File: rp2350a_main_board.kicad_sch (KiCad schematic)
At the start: 65 parts, among them J1 USB_C_Receptacle_USB2.0_16P, J2 Micro_SD_Card_Det1, J3 Conn_02x10_Odd_Even, J4 SM03B-SRSS-TB, J5 SM03B-SRSS-TB, J6 Conn_02x10_Odd_Even, SW1 SW_Push, SW2 SW_Push, U1 RP2350_60QFN, U2 W25Q16JVSS, U3 APS1604M-3SQRx-SN, U4 AP2112K-3.3, Y1 ABM8-272-T3

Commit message: V1.0.0
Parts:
- removed C12: 100n, Capacitor_SMD:C_0402_1005Metric_Pad0.74x0.62mm_HandSolder, symbol Device:C
- removed C24: 10u, Capacitor_SMD:C_0603_1608Metric_Pad1.08x0.95mm_HandSolder, symbol Device:C
- removed J3, J6: Conn_02x10_Odd_Even, Connector_PinSocket_2.54mm:PinSocket_2x10_P2.54mm_Vertical, symbol Connector_Generic:Conn_02x10_Odd_Even
- removed RN1, RN2: 10k, Resistor_SMD:R_Array_Convex_4x0603, symbol Device:R_Pack04_Split
- removed U4: AP2112K-3.3, Package_TO_SOT_SMD:SOT-23-5, symbol Regulator_Linear:AP2112K-3.3
- added J3, J6: Conn_02x12, Connector_PinSocket_2.54mm:PinSocket_2x12_P2.54mm_Vertical, symbol Connector_Generic:Conn_02x12_Odd_Even
- added J7, J8: Conn_02x12, Connector_PinSocket_2.54mm:PinSocket_2x12_P2.54mm_Vertical_SMD, symbol Connector_Generic:Conn_02x12_Odd_Even
- added L2: 470n, Library:Inductor_SMD_L_4.0x4.0_H1.5, symbol Device:L
- added R20: 511k, Resistor_SMD:R_0402_1005Metric_Pad0.72x0.64mm_HandSolder, symbol Device:R
- added R21: 91k, Resistor_SMD:R_0402_1005Metric_Pad0.72x0.64mm_HandSolder, symbol Device:R
- added R22, R23, R24: 10k, Resistor_SMD:R_0402_1005Metric_Pad0.72x0.64mm_HandSolder, symbol Device:R
- added R25: 33k, Resistor_SMD:R_0402_1005Metric_Pad0.72x0.64mm_HandSolder, symbol Device:R
- added SW3: SW_SPDT, Button_Switch_SMD:SW_SPDT_CK_JS102011SAQN, symbol Switch:SW_SPDT
- added TP1: ST, TestPoint:TestPoint_Pad_D1.0mm, symbol Connector:TestPoint
- added TP2: EN, TestPoint:TestPoint_Pad_D1.0mm, symbol Connector:TestPoint
- added TP4: PG, TestPoint:TestPoint_Pad_D1.0mm, symbol Connector:TestPoint
- added U4: TPS63802, Library:TPS63802, symbol New_Library:TPS63802
- added U5: TPS2116DRL, Package_TO_SOT_SMD:SOT-583-8, symbol Power_Management:TPS2116DRL
- C3, C4: footprint Capacitor_SMD:C_0603_1608Metric_Pad1.08x0.95mm_HandSolder -> Capacitor_SMD:C_0402_1005Metric_Pad0.74x0.62mm_HandSolder
- D1, D2: footprint LED_SMD:LED_0805_2012Metric -> LED_SMD:LED_0805_2012Metric_Pad1.15x1.40mm_HandSolder
- R1, R2, R6: footprint Resistor_SMD:R_0805_2012Metric_Pad1.20x1.40mm_HandSolder -> Resistor_SMD:R_0402_1005Metric_Pad0.72x0.64mm_HandSolder
- R11: value 470 -> 1k; footprint Resistor_SMD:R_0603_1608Metric_Pad0.98x0.95mm_HandSolder -> Resistor_SMD:R_0402_1005Metric_Pad0.72x0.64mm_HandSolder
- R7, R8, R9: footprint Resistor_SMD:R_0805_2012Metric_Pad1.20x1.40mm_HandSolder -> Resistor_SMD:R_0402_1005Metric_Pad0.72x0.64mm_HandSolder; now in the parts list
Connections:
- net +3V3: now also C22.1, J3.1 (Pin_1), J3.2 (Pin_2), J3.3 (Pin_3), J3.4 (Pin_4), J6.7 (Pin_7), J6.8 (Pin_8), J7.1 (Pin_1), J7.2 (Pin_2), J7.3 (Pin_3), J7.4 (Pin_4), J8.7 (Pin_7), J8.8 (Pin_8), R20.1, U4.6 (VOUT)
- net GND: now also J3.11 (Pin_11), J3.12 (Pin_12), J3.17 (Pin_17), J3.18 (Pin_18), J3.23 (Pin_23), J3.24 (Pin_24), J3.5 (Pin_5), J3.6 (Pin_6), J6.13 (Pin_13), J6.14 (Pin_14), J6.19 (Pin_19), J6.20 (Pin_20), J6.23 (Pin_23), J6.24 (Pin_24), J7.11 (Pin_11), J7.12 (Pin_12), J7.17 (Pin_17), J7.18 (Pin_18), J7.23 (Pin_23), J7.24 (Pin_24), J7.5 (Pin_5), J7.6 (Pin_6), J8.13 (Pin_13), J8.14 (Pin_14), J8.19 (Pin_19), J8.20 (Pin_20), J8.23 (Pin_23), J8.24 (Pin_24), R21.2, R24.2, U4.2 (MODE), U4.3 (AGND), U4.8 (GND), U5.1 (GND); no longer U1.15 (GPIO11), U1.17 (GPIO13), U1.19 (GPIO15), U1.28 (GPIO17), U1.31 (GPIO19)
- net GPIO10: now also J3.10 (Pin_10), J7.10 (Pin_10)
- net GPIO12: now also J3.14 (Pin_14), J7.14 (Pin_14)
- net GPIO14: now also J3.16 (Pin_16), J7.16 (Pin_16)
- net GPIO16: now also J3.20 (Pin_20), J7.20 (Pin_20)
- net GPIO18: now also J3.22 (Pin_22), J7.22 (Pin_22)
- net GPIO20: now also J6.21 (Pin_21), J8.21 (Pin_21)
- net GPIO21: now also J6.22 (Pin_22), J8.22 (Pin_22)
- net GPIO22: now also J6.17 (Pin_17), J8.17 (Pin_17)
- net GPIO23: now also J6.18 (Pin_18), J8.18 (Pin_18)
- net GPIO24: now also J6.15 (Pin_15), J8.15 (Pin_15)
- net GPIO25: now also J6.16 (Pin_16), J8.16 (Pin_16)
- net GPIO26_ADC0: now also J6.11 (Pin_11), J8.11 (Pin_11)
- net GPIO27_ADC1: now also J6.12 (Pin_12), J8.12 (Pin_12)
- net GPIO28_ADC2: now also J6.9 (Pin_9), J8.9 (Pin_9)
- net GPIO29_ADC3: now also J6.10 (Pin_10), J8.10 (Pin_10)
- net GPIO9: now also J3.7 (Pin_7), J7.7 (Pin_7)
- net RUN: now also J3.8 (Pin_8), J7.8 (Pin_8)
- net VBUS renamed VUSB
- net VUSB: now also J6.1 (Pin_1), J6.2 (Pin_2), J8.1 (Pin_1), J8.2 (Pin_2), R25.1, U5.3 (VIN1), U5.5 (MODE); no longer C21.1, C22.1
- new net: R20.2, R21.1, U4.4 (FB)
- new net: R22.2, TP2.1, U4.1 (EN)
- new net: TP4.1, U4.5 (PG)
- new net: R23.1, SW3.1 (A), U5.2 (VOUT), U5.7 (VOUT)
- new net: R24.1, R25.2, U5.4 (PR1)
- new net: R23.2, TP1.1, U5.8 (ST)
- new net GPIO11: J3.9 (Pin_9), J7.9 (Pin_9), U1.15 (GPIO11)
- new net GPIO13: J3.13 (Pin_13), J7.13 (Pin_13), U1.17 (GPIO13)
- new net GPIO15: J3.15 (Pin_15), J7.15 (Pin_15), U1.19 (GPIO15)
- new net GPIO17: J3.19 (Pin_19), J7.19 (Pin_19), U1.28 (GPIO17)
- new net GPIO19: J3.21 (Pin_21), J7.21 (Pin_21), U1.31 (GPIO19)
- new net PS_L1: L2.1, U4.9 (L1)
- new net PS_L2: L2.2, U4.7 (L2)
- new net VBAT: J6.3 (Pin_3), J6.4 (Pin_4), J8.3 (Pin_3), J8.4 (Pin_4), U5.6 (VIN2)
- new net VIN: C21.1, J6.5 (Pin_5), J6.6 (Pin_6), J8.5 (Pin_5), J8.6 (Pin_6), R22.1, SW3.2 (B), U4.10 (VIN)
- no-connect marks 4 -> 3
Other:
- note added: "Power"
- note added: "Power Selection"
- note removed: "Power (placeholder)"
- moved on the sheet: R13, R14, R15, R16, R17, R18, R19

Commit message: Clean up component references
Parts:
- renumbered C21 to C1, C14 to C10, C15 to C11, C16 to C12, C17 to C13, C18 to C14, C19 to C15, C1 to C16, C8 to C17, C7 to C18, C6 to C19, C22 to C2, C2 to C20, C4 to C21, C3 to C22, C23 to C3, C5 to C4, C20 to C5, C9 to C6, C10 to C7, C11 to C8, C13 to C9, J5 to J2, J2 to J3, J3 to J5, L2 to L1, L1 to L2, R22 to R1, R2 to R10, R16 to R11, R19 to R12, R11 to R13, R25 to R14, R12 to R15, R23 to R16, R24 to R17, R5 to R18, R3 to R19, R17 to R2, R4 to R20, R10 to R21, R6 to R22, R9 to R23, R7 to R24, R8 to R25, R20 to R3, R18 to R4, R14 to R5, R21 to R6, R13 to R7, R15 to R8, R1 to R9, SW3 to SW1, SW1 to SW2, SW2 to SW3, TP2 to TP1, TP4 to TP2, TP1 to TP3, U4 to U1, U5 to U2, U2 to U3, U1 to U4, U3 to U5

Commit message: Update BOM list
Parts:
- R12, R21, R22: now in the parts list
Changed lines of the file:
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@@
 		(unit 1)
 		(exclude_from_sim no)
-		(in_bom no)
+		(in_bom yes)
 		(on_board yes)
 		(dnp no)
@@
 		(unit 1)
 		(exclude_from_sim no)
-		(in_bom no)
+		(in_bom yes)
 		(on_board yes)
 		(dnp no)
@@
 		(unit 1)
 		(exclude_from_sim no)
-		(in_bom no)
+		(in_bom yes)
 		(on_board yes)
 		(dnp no)

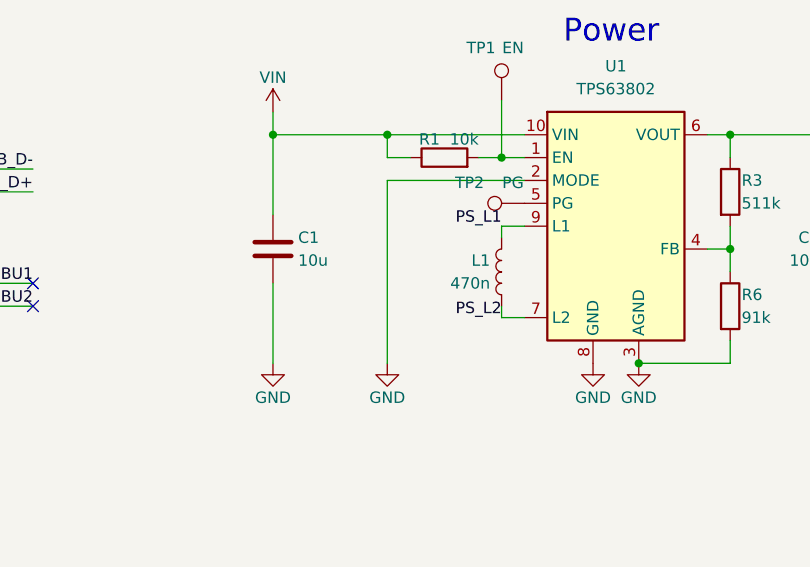
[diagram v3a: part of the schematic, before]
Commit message: Add text, Add part name to L1
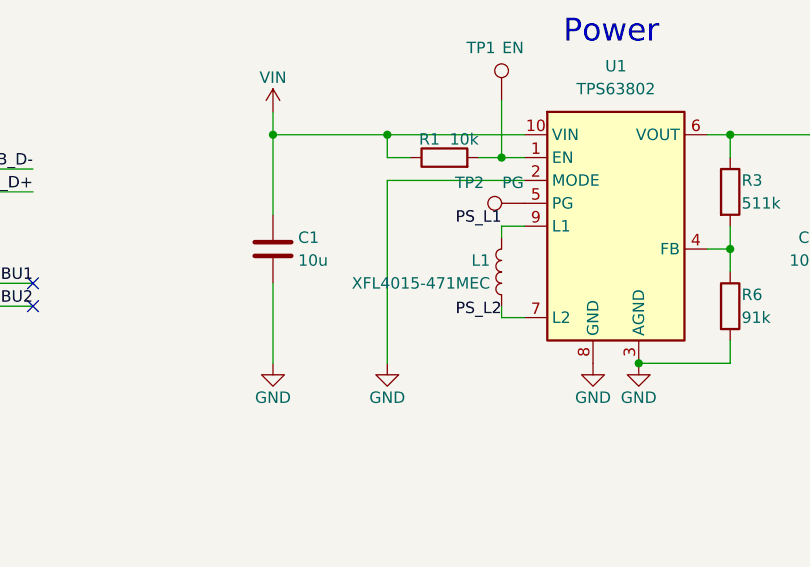
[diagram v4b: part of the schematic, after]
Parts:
- L1: value 470n -> XFL4015-471MEC
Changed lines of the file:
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@@
 			)
 		)
-		(property "Value" "470n"
+		(property "Value" "XFL4015-471MEC"
 			(at 123.19 55.8799 0)
 			(effects
